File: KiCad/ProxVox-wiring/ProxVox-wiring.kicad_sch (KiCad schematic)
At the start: 0 parts

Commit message: wiring for power button added
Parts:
- added P1: ~, symbol ProxVox-wiring:IDC10_PLUG@10
- added SW1: Alps (original), symbol Switch:SW_Push
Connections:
- new net HDD LED (+): P1.1
- new net HDD LED (-): P1.3
- new net Power LED (+): P1.2
- new net Power LED (-): P1.4
- new net Power Switch (+): P1.6, SW1.1
- new net Power Switch (-): P1.8, SW1.2
- new net Reset Switch (+): P1.7
- new net Reset Switch (-): P1.5
- no-connect marks 0 -> 8
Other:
- note added: "To Motherboard PANEL connector"

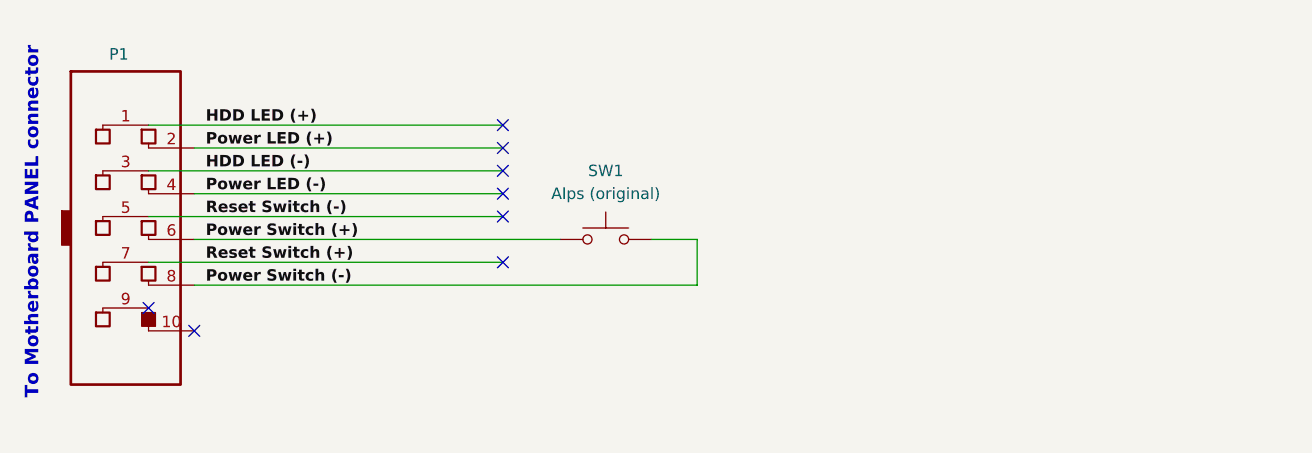
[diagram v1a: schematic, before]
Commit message: Pictorial circuit diagram of audio amplifier started
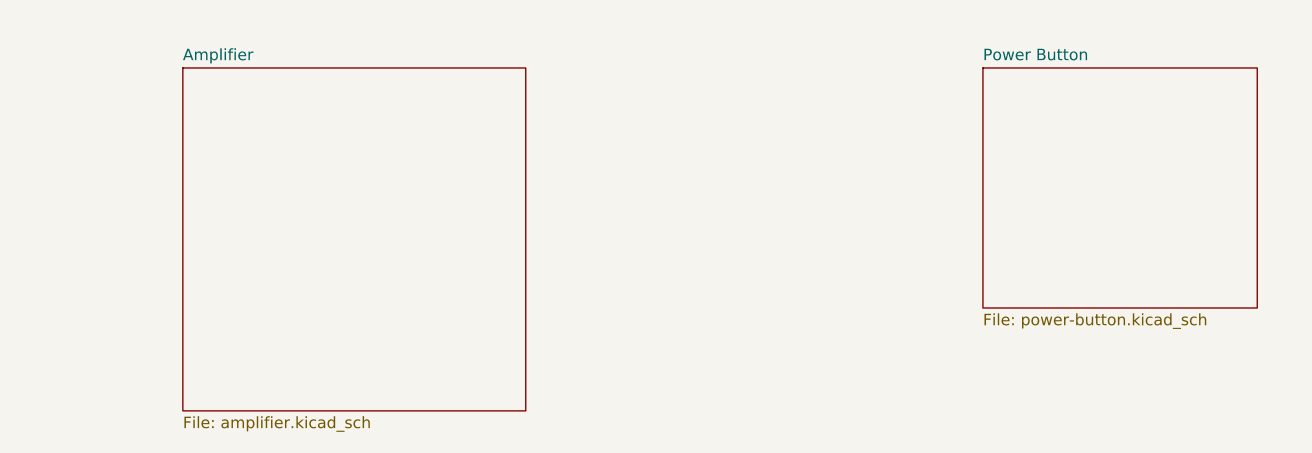
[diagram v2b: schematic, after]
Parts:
- removed P1: ~, symbol ProxVox-wiring:IDC10_PLUG@10
- removed SW1: Alps (original), symbol Switch:SW_Push
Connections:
- no-connect marks 8 -> 0
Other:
- added sheet Amplifier (amplifier.kicad_sch)
- added sheet Power Button (power-button.kicad_sch)
- note removed: "To Motherboard PANEL connector"
